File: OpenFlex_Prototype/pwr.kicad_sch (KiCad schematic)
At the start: 8 parts, among them U4 LM2940S-5.0

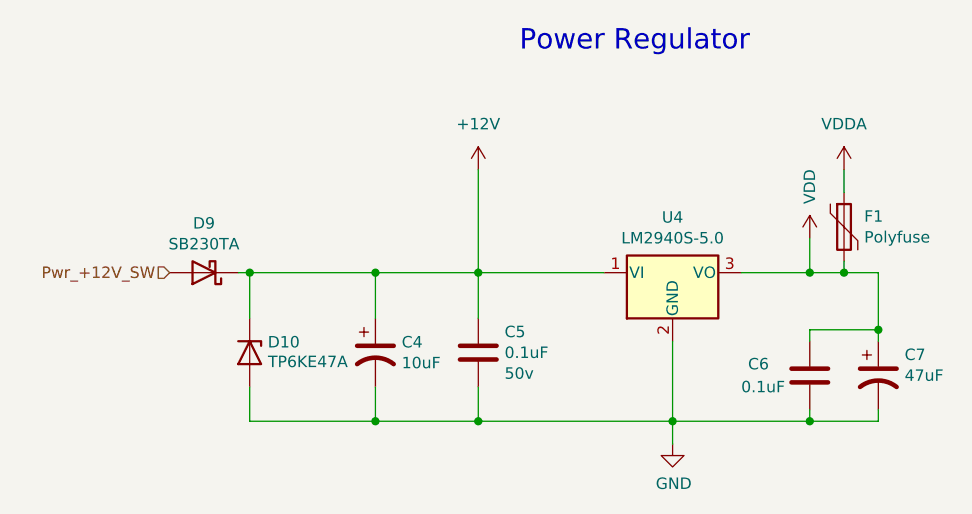
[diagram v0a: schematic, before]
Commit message: Updated PCB to ESP32-S2-Devkit-C1
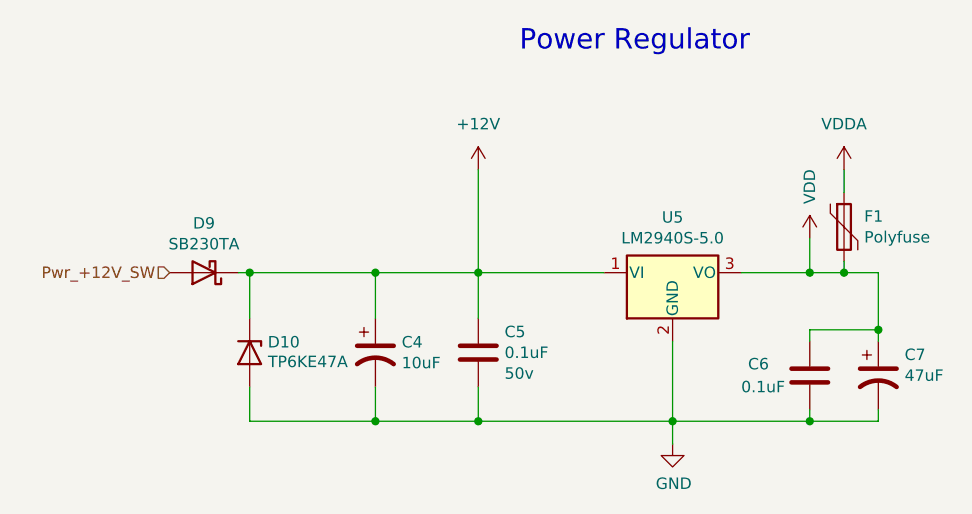
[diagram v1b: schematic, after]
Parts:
- renumbered U4 to U5

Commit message: Updated Sourcing for prototype
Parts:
- C4: Digikey Part Number P10316-ND -> (none)
- F1: footprint Fuse:Fuse_BelFuse_0ZRE0055FF_L14.0mm_W4.1mm -> Fuse:Fuse_BelFuse_0ZRE0005FF_L8.3mm_W3.8mm; Digikey Part Number 507-2403-ND -> (none); URL https://www.digikey.com.au/product-detail/en/bel-fuse-inc/0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 -> (none)
- U5: Digikey Part Number NCV7805BTGOS-ND -> (none); Mouser_Part_Number 863-NCV7805BTG -> 863-NCV7805BTG; URL https://www.digikey.com.au/product-detail/en/on-semiconduct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 -> https://www.mouser.fr/ProductDetail/onsemi/NCV7805BTG?qs=8s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
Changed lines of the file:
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@@
-			)
-		)
-		(property "Digikey Part Number" "P10316-ND"
-			(at 0 130.81 0)
-			(hide yes)
-			(show_name no)
-			(do_not_autoplace no)
-			(effects
-				(font
-					(size 1.27 1.27)
-				)
 			)
 		)
@@
 			)
 		)
-		(property "Digikey Part Number" "NCV7805BTGOS-ND"
-			(at 0 111.76 0)
-			(hide yes)
-			(show_name no)
-			(do_not_autoplace no)
-			(effects
-				(font
-					(size 1.27 1.27)
-				)
-			)
-		)
 		(property "Manufacturer_Name" "ON Semi"
 			(at 0 111.76 0)
@@
 			)
 		)
-		(property "URL" "https://www.digikey.com.au/product-detail/en/on-semiconductor/NCV7805BTG/NCV7805BTGOS-ND/921437"
+		(property "URL" "https://www.mouser.fr/ProductDetail/onsemi/NCV7805BTG?qs=8sOby8ZxZLE6UfUj5jjWgw%3D%3D"
 			(at 0 111.76 0)
 			(hide yes)
@@
 			)
 		)
-		(property "Mouser_Part_Number" "863-NCV7805BTG "
+		(property "Mouser_Part_Number" "863-NCV7805BTG"
 			(at 161.29 49.53 0)
 			(hide yes)
@@
 			)
 		)
-		(property "Footprint" "Fuse:Fuse_BelFuse_0ZRE0055FF_L14.0mm_W4.1mm"
+		(property "Footprint" "Fuse:Fuse_BelFuse_0ZRE0005FF_L8.3mm_W3.8mm"
 			(at 181.61 49.53 0)
 			(hide yes)
@@
 			)
 		)
-		(property "Digikey Part Number" "507-2403-ND"
-			(at 0 102.87 0)
-			(hide yes)
-			(show_name no)
-			(do_not_autoplace no)
-			(effects
-				(font
-					(size 1.27 1.27)
-				)
-			)
-		)
 		(property "Manufacturer_Name" "Bel Fuse"
 			(at 0 102.87 0)
@@
 			(at 0 102.87 0)
 			(hide yes)
-			(show_name no)
-			(do_not_autoplace no)
-			(effects
-				(font
-					(size 1.27 1.27)
-				)
-			)
-		)
-		(property "URL" "https://www.digikey.com.au/product-detail/en/bel-fuse-inc/0ZRP0050FF1E/507-2403-ND/9468252"
-			(at 0 102.87 0)
-			(hide yes)

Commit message: Enclosure WIP
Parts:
- C7: Digikey Part Number P19658CT-ND -> (none)
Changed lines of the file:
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@@
-			)
-		)
-		(property "Digikey Part Number" "P19658CT-ND"
-			(at 0 133.35 0)
-			(hide yes)
-			(show_name no)
-			(do_not_autoplace no)
-			(effects
-				(font
-					(size 1.27 1.27)
-				)
 			)
 		)

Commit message: Updated BOM
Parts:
- D9: value SB230TA -> SB230-E3/54; Digikey Part Number 1655-1518-1-ND -> (none); Manufacturer_Name SMC -> Vishay Semiconductors; Manufacturer_Part_Number SB230TA -> SB230-E3/54; Mouser URL https://www.mouser.fr/ProductDetail/Micro-Commercial-Compon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 -> https://www.mouser.fr/ProductDetail/Vishay-Semiconductors/S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; Mouser_Part_Number 833-SB230-TP -> 625-SB230-E3; URL https://www.digikey.com.au/product-detail/en/smc-diode-solu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 -> (none)
- U5: Manufacturer_Name ON Semi -> Texas Instruments; Manufacturer_Part_Number NCV7805BTG -> LM2940T-5.0/LF08; Mouser_Part_Number 863-NCV7805BTG -> 926-LM2940T-50/LF08; URL https://www.mouser.fr/ProductDetail/onsemi/NCV7805BTG?qs=8s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 -> https://www.mouser.fr/ProductDetail/Texas-Instruments/LM294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
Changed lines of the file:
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@@
 			)
 		)
-		(property "Value" "SB230TA"
+		(property "Value" "SB230-E3/54"
 			(at 109.22 46.355 0)
 			(show_name no)
@@
 			)
 		)
-		(property "Datasheet" "https://www.mouser.com/datasheet/2/115/ds13002-60388.pdf"
+		(property "Datasheet" "https://www.vishay.com/doc?88717"
 			(at 109.22 49.53 0)
 			(hide yes)
@@
 			)
 		)
-		(property "Digikey Part Number" "1655-1518-1-ND"
+		(property "Manufacturer_Name" "Vishay Semiconductors"
 			(at 254 -12.7 0)
 			(hide yes)
@@
 			)
 		)
-		(property "Manufacturer_Name" "SMC"
+		(property "Manufacturer_Part_Number" "SB230-E3/54"
 			(at 254 -12.7 0)
 			(hide yes)
@@
 			)
 		)
-		(property "Manufacturer_Part_Number" "SB230TA"
-			(at 254 -12.7 0)
-			(hide yes)
-			(show_name no)
-			(do_not_autoplace no)
-			(effects
-				(font
-					(size 1.27 1.27)
-				)
-			)
-		)
-		(property "URL" "https://www.digikey.com.au/product-detail/en/smc-diode-solutions/SB230TA/1655-1518-1-ND/6022963"
-			(at 254 -12.7 0)
-			(hide yes)
-			(show_name no)
-			(do_not_autoplace no)
-			(effects
-				(font
-					(size 1.27 1.27)
-				)
-			)
-		)
-		(property "Mouser_Part_Number" "833-SB230-TP "
+		(property "Mouser_Part_Number" "625-SB230-E3"
 			(at 109.22 49.53 0)
 			(hide yes)
@@
 			)
 		)
-		(property "Mouser URL" "https://www.mouser.fr/ProductDetail/Micro-Commercial-Components-MCC/SB230-TP?qs=P1JMDcb91o64q2VtM2oH0Q%3D%3D"
+		(property "Mouser URL" "https://www.mouser.fr/ProductDetail/Vishay-Semiconductors/SB230-E3-54?qs=u91jd7aysvMVfxBBDX1%252BYQ%3D%3D"
 			(at 109.22 49.53 0)
 			(hide yes)
@@
 			)
 		)
-		(property "Manufacturer_Name" "ON Semi"
+		(property "Manufacturer_Name" "Texas Instruments"
 			(at 0 111.76 0)
 			(hide yes)
@@
 			)
 		)
-		(property "Manufacturer_Part_Number" "NCV7805BTG"
+		(property "Manufacturer_Part_Number" "LM2940T-5.0/LF08"
 			(at 0 111.76 0)
 			(hide yes)
@@
 			)
 		)
-		(property "URL" "https://www.mouser.fr/ProductDetail/onsemi/NCV7805BTG?qs=8sOby8ZxZLE6UfUj5jjWgw%3D%3D"
+		(property "URL" "https://www.mouser.fr/ProductDetail/Texas-Instruments/LM2940T-5.0-LF08?qs=X1J7HmVL2ZHslyM5jzTq7g%3D%3D"
 			(at 0 111.76 0)
 			(hide yes)
@@
 			)
 		)
-		(property "Mouser_Part_Number" "863-NCV7805BTG"
+		(property "Mouser_Part_Number" "926-LM2940T-50/LF08"
 			(at 161.29 49.53 0)
 			(hide yes)
